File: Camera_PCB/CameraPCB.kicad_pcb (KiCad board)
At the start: 6 copper layers, 65.6 x 55 mm, 173 parts, among them J1 MIPI-CSI2, J2 USB_A, J3 SDA, J4 UART_0, J5 UART_2, J6 USB_C_Receptacle_PowerOnly_6P, SW1 PWR, SW2 RST, U1 AXP203, U2 V3s-eLQFP128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

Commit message: Pre sd-card move
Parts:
- moved TP31 1.58 mm to (154.2, 82.8)
- moved C17 0.50 mm to (163.3, 101.0)
- moved J4 0.05 mm to (139.2, 66.0)
- moved J5 0.05 mm to (130.3, 66.0)
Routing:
- net HPVCC: track 105.5 -> 108.8 mm
- net VIPS: track 44.6 -> 47.6 mm, vias 22 -> 23
- net GND: track 18.4 -> 20.7 mm, vias 169 -> 215
- net AVCC: track 7.21 -> 8.30 mm
- net VBUS: track 32.3 -> 33.1 mm
- net SDC0_CMD: track 50.1 -> 49.3 mm
- net TWI0_SCK: track 68.2 -> 68.9 mm, vias 2 -> 1
- net SDC0_D0: track 52.4 -> 51.7 mm
- net TWI0_SDA: track 66.0 -> 66.6 mm, vias 2 -> 1
- net IRQ: vias 2 -> 1

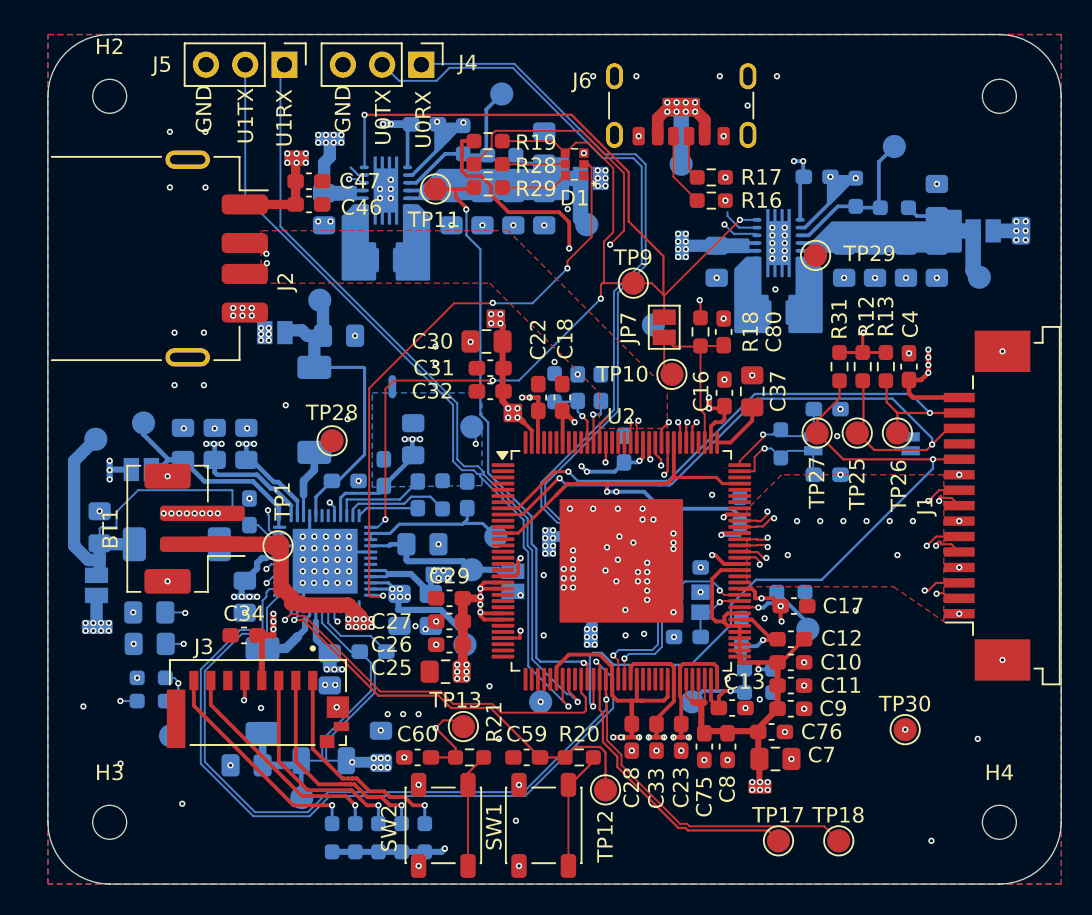
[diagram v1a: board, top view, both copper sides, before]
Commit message: Added 3d models, completed layout. Should still review more.
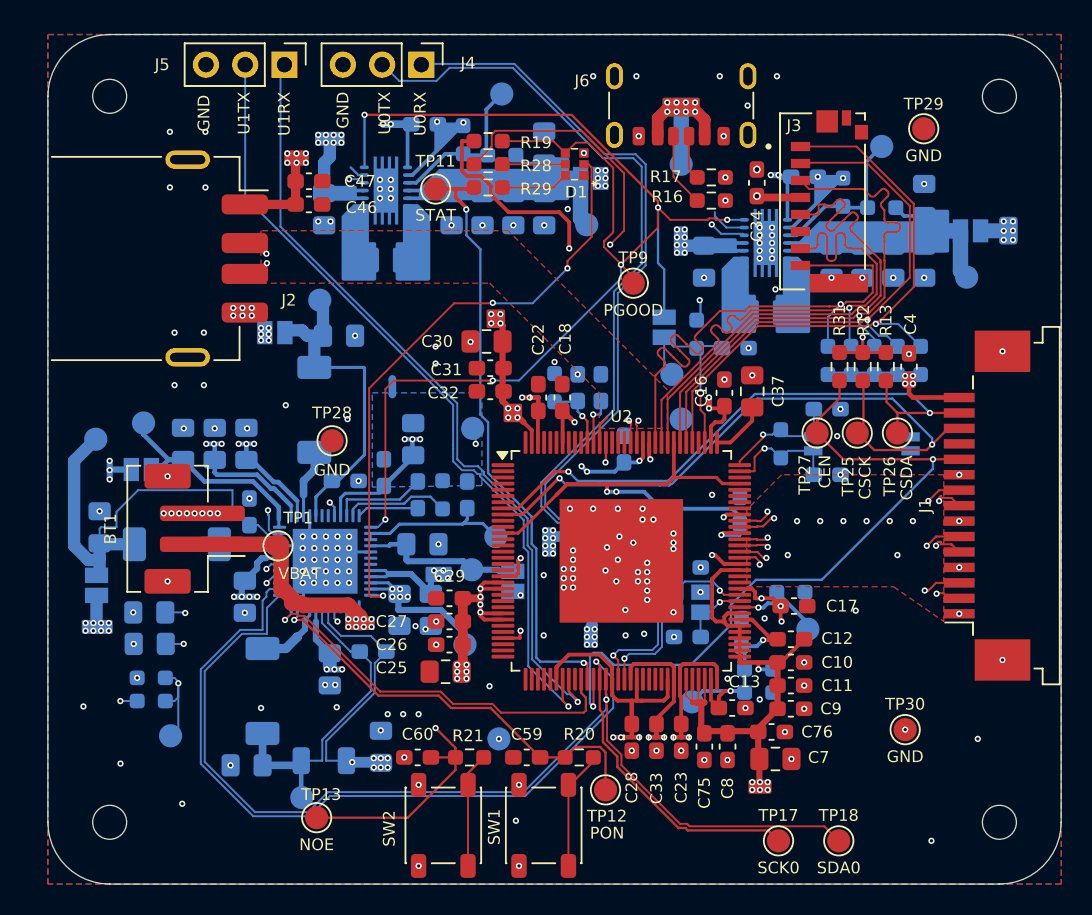
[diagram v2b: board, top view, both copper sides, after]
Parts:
- C80, JP7, R18, TP10: moved to B.Cu
- TP16: value 3.0V -> NVEN
- TP7: value 3.0V -> 3V0
- moved J3 48.9 mm to (165.2, 74.8), turned to 90 degrees
- moved R2 44.6 mm to (171.5, 85.1)
- moved R3 44.6 mm to (170.0, 85.1)
- moved R4 44.6 mm to (167.0, 85.1)
- moved R5 44.6 mm to (168.5, 85.1)
- moved R6 44.6 mm to (165.5, 85.1)
- moved C34 44.3 mm to (160.9, 73.6), turned to 90 degrees
- moved TP13 11.2 mm to (132.4, 114.7)
- moved TP29 10.8 mm to (171.7, 70.1)
- moved TP31 6.36 mm to (156.0, 88.9)
- moved TP32 3.61 mm to (144.2, 109.6)
- moved C80 1.29 mm to (159.5, 84.3), turned to 0 degrees
- moved C2 0.82 mm to (164.0, 73.2)
- moved C3 0.82 mm to (157.5, 78.7)
- moved C68 0.82 mm to (165.7, 78.7)
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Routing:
- net SDC0_D0: track 51.7 -> 36.6 mm, vias 2 -> 1
- net SDC0_CLK: track 48.4 -> 34.1 mm, vias 2 -> 0
- net SDC0_D1: track 51.2 -> 37.0 mm, vias 2 -> 1
- net SDC0_CMD: track 49.3 -> 36.4 mm, vias 2 -> 1
- net SDC0_D3: track 49.2 -> 36.5 mm, vias 2 -> 1
- net SDC0_D2: track 48.4 -> 38.2 mm, vias 2 -> 1
- net Net-(U1-N_OE): track 24.2 -> 33.0 mm
- net HPVCC: track 108.8 -> 101.5 mm, vias 37 -> 34
- net PGOOD: track 87.9 -> 88.8 mm, vias 5 -> 6
- net PWREN: track 69.5 -> 68.7 mm
- net VBAT: track 47.0 -> 46.4 mm
- net RESET: track 13.5 -> 13.1 mm, vias 0 -> 1
- net GND: vias 215 -> 216

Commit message: ordered PCB V1.0
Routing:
- net GND: vias 216 -> 225
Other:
- board text added: "Purdue ECE Senior Design Group 25, Semi-Truck Backup Camera PCB V1.0 Nov-10-2025"
- board text added: "U2RX"
- board text added: "U2TX"
- board text removed: "U1RX"
- board text removed: "U1TX"
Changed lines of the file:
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@@
 			)
 		)
-		(property "Datasheet" "~"
+		(property "Datasheet" "https://www.te.com/usa-en/product-1-84952-5.datasheet.pdf"
 			(at 0 0 90)
 			(unlocked yes)
@@
 			)
 		)
-		(property "Description" "Generic connectable mounting pin connector, single row, 01x15, script generated (kicad-library-utils/schlib/autogen/connector/)"
+		(property "Description" "15 Position FPC Connector Contacts, Bottom 0.039\" (1.00mm) Surface Mount, Right Angle"
 			(at 0 0 90)
 			(unlocked yes)
@@
 		(layer "Edge.Cuts")
 	)
-	(gr_text "U1TX"
+	(gr_text "U2TX"
 		(at 127.7 67.7 90)
 		(layer "F.SilkS")
@@
 	)
 	(gr_text "GND"
-		(at 125.1 67.9 90)
+		(at 125.3 67.7 90)
 		(layer "F.SilkS")
 		(effects
@@
 		)
 	)
+	(gr_text "Purdue ECE Senior Design\nGroup 25, Semi-Truck\nBackup Camera PCB \nV1.0 Nov-10-2025"
+		(at 125.9 111 0)
+		(layer "F.SilkS")
+		(effects
+			(font
+				(size 1 1)
+				(thickness 0.2)
+				(bold yes)
+			)
+			(justify bottom)
+		)
+	)
 	(gr_text "U0RX"
 		(at 139.1 67.7 90)
@@
 		)
 	)
-	(gr_text "U1RX"
+	(gr_text "U2RX"
 		(at 130.3 67.7 90)
 		(layer "F.SilkS")
@@
 	)
 	(via
+		(at 171.7 70.1)
+		(size 0.4064)
+		(drill 0.2032)
+		(layers "F.Cu" "B.Cu")
+		(net 9)
+	)
+	(via
 		(at 149.3 86)
 		(size 0.4064)
@@
 	)
 	(via
+		(at 178.2 95.4)
+		(size 0.4064)
+		(drill 0.2032)
+		(layers "F.Cu" "B.Cu")
+		(free yes)
+		(net 9)
+	)
+	(via
 		(at 133.75 99.5)
 		(size 0.4064)
@@
 	)
 	(via
+		(at 147.9 66.4)
+		(size 0.4064)
+		(drill 0.2032)
+		(layers "F.Cu" "B.Cu")
+		(free yes)
+		(net 9)
+	)
+	(via
 		(at 133.75 98)
 		(size 0.4064)
@@
 	)
 	(via
+		(at 136.2 84.9)
+		(size 0.4064)
+		(drill 0.2032)
+		(layers "F.Cu" "B.Cu")
+		(net 9)
+	)
+	(via
 		(at 142.3625 83.9)
 		(size 0.4064)
@@
 	)
 	(via
+		(at 156.2 117.7)
+		(size 0.4064)
+		(drill 0.2032)
+		(layers "F.Cu" "B.Cu")
+		(free yes)
+		(net 9)
+	)
+	(via
 		(at 126 95)
 		(size 0.4064)
@@
 	)
 	(via
-		(at 166.5 95.5)
-		(size 0.4064)
-		(drill 0.2032)
-		(layers "F.Cu" "B.Cu")
-		(free yes)
-		(net 9)
-	)
-	(via
 		(at 120.78 105.65)
 		(size 0.4064)
@@
 	)
 	(via
-		(at 134.5 99.5)
+		(at 177.6 71.9)
 		(size 0.4064)
 		(drill 0.2032)
 		(layers "F.Cu" "B.Cu")
+		(free yes)
 		(net 9)
 	)
 	(via
-		(at 152 96.5)
+		(at 134.5 99.5)
 		(size 0.4064)
 		(drill 0.2032)
@@
 	)
 	(via
-		(at 122.75 99.4)
+		(at 152 96.5)
 		(size 0.4064)
 		(drill 0.2032)
@@
 	)
 	(via
-		(at 165 95.5)
+		(at 122.75 99.4)
 		(size 0.4064)
 		(drill 0.2032)
 		(layers "F.Cu" "B.Cu")
-		(free yes)
 		(net 9)
 	)
@@
 	)
 	(via
+		(at 154.9 91.8)
+		(size 0.4064)
+		(drill 0.2032)
+		(layers "F.Cu" "B.Cu")
+		(net 9)
+	)
+	(via
+		(at 150.3 91.5)
+		(size 0.4064)
+		(drill 0.2032)
+		(layers "F.Cu" "B.Cu")
+		(net 9)
+	)
+	(via
 		(at 123.5 95)
 		(size 0.4064)
@@
 	)
 	(via
+		(at 170.3 114.5)
+		(size 0.4064)
+		(drill 0.2032)
+		(layers "F.Cu" "B.Cu")
+		(free yes)
+		(net 9)
+	)
+	(via
 		(at 166.3125 88.25)
 		(size 0.4064)
@@
 	)
 	(via
-		(at 169.5 95.5)
+		(at 137 108)
 		(size 0.4064)
 		(drill 0.2032)
@@
 	)
 	(via
-		(at 137 108)
+		(at 166.3125 92.5)
 		(size 0.4064)
 		(drill 0.2032)
 		(layers "F.Cu" "B.Cu")
-		(free yes)
 		(net 9)
 	)
 	(via
-		(at 166.3125 92.5)
+		(at 154.4 110.3625)
 		(size 0.4064)
 		(drill 0.2032)
@@
 	)
 	(via
-		(at 154.4 110.3625)
+		(at 176.8 104.49)
 		(size 0.4064)
 		(drill 0.2032)
@@
 	)
 	(via
-		(at 176.8 104.49)
+		(at 163.9625 106.15)
 		(size 0.4064)
 		(drill 0.2032)
@@
 	)
 	(via
-		(at 163.9625 106.15)
+		(at 178 80.3)
 		(size 0.4064)
 		(drill 0.2032)
 		(layers "F.Cu" "B.Cu")
+		(free yes)
 		(net 9)
 	)
@@
 	)
 	(via
-		(at 168 95.5)
+		(at 155.5375 103)
 		(size 0.4064)
 		(drill 0.2032)
 		(layers "F.Cu" "B.Cu")
-		(free yes)
 		(net 9)
 	)
 	(via
-		(at 155.5375 103)
+		(at 152.8 110.3625)
 		(size 0.4064)
 		(drill 0.2032)
@@
 	)
 	(via
-		(at 152.8 110.3625)
+		(at 116.7 78.3)
 		(size 0.4064)
 		(drill 0.2032)
 		(layers "F.Cu" "B.Cu")
+		(free yes)
 		(net 9)
 	)
@@
 	)
 	(via
+		(at 122.3 78.3)
+		(size 0.4064)
+		(drill 0.2032)
+		(layers "F.Cu" "B.Cu")
+		(free yes)
+		(net 9)
+	)
+	(via
 		(at 137.2 74.6)
 		(size 0.4064)
@@
 	)
 	(via
+		(at 130.1 117.1)
+		(size 0.4064)
+		(drill 0.2032)
+		(layers "F.Cu" "B.Cu")
+		(free yes)
+		(net 9)
+	)
+	(via
 		(at 158.75 70.58)
 		(size 0.4064)
@@
 	)
 	(segment
-		(start 131.52812 100.942)
-		(end 134.442 100.942)
-		(width 1)
-		(layer "F.Cu")
-		(net 11)
-	)
-	(segment
-		(start 130.7812 100.455705)
-		(end 130.7812 100.8138)
+		(start 134.442 100.942)
+		(end 135.2 101.7)
 		(width 1)
 		(layer "F.Cu")
@@
 	)
 	(segment
-		(start 130.294295 99.9688)
-		(end 130.7812 100.455705)
+		(start 131.3138 100.8138)
+		(end 131.39992 100.8138)
 		(width 1)
 		(layer "F.Cu")
@@
 	)
 	(segment
-		(start 135.2 101.7)
-		(end 135.2 102.1)
+		(start 125 97)
+		(end 129.8 97)
 		(width 1)
 		(layer "F.Cu")
@@
 	)
 	(segment
-		(start 130.1 99.9688)
-		(end 130.294295 99.9688)
+		(start 130.1 99.6)
+		(end 131.3138 100.8138)
 		(width 1)
 		(layer "F.Cu")
@@
 	)
 	(segment
-		(start 134.442 100.942)
-		(end 135.2 101.7)
+		(start 129.8 97)
+		(end 130.1 97.3)
 		(width 1)
 		(layer "F.Cu")
@@
 	)
 	(segment
-		(start 131.39992 100.8138)
-		(end 131.52812 100.942)
+		(start 131.52812 100.942)
+		(end 134.442 100.942)
 		(width 1)
 		(layer "F.Cu")
@@
 	(segment
 		(start 130.1 97.3)
-		(end 130.1 99.9688)
+		(end 130.1 99.6)
 		(width 1)
 		(layer "F.Cu")
@@
 	)
 	(segment
-		(start 130.7812 100.8138)
-		(end 131.39992 100.8138)
-		(width 1)
-		(layer "F.Cu")
-		(net 11)
-	)
-	(segment
-		(start 129.8 97)
-		(end 130.1 97.3)
+		(start 131.39992 100.8138)
+		(end 131.52812 100.942)
 		(width 1)
 		(layer "F.Cu")
@@
 	)
 	(segment
-		(start 125 97)
-		(end 129.8 97)
+		(start 135.2 101.7)
+		(end 135.2 102.1)
 		(width 1)
 		(layer "F.Cu")
@@
 	)
 	(segment
+		(start 116.7 93.8)
+		(end 116.7 91.6)
+		(width 0.8)
+		(layer "B.Cu")
+		(net 137)
+	)
+	(segment
 		(start 120.6 97)
 		(end 118.6125 97)
@@
 	(segment
 		(start 116.7 97.1)
-		(end 116.7 91.6)
+		(end 116.7 93.8)
 		(width 0.8)
 		(layer "B.Cu")
